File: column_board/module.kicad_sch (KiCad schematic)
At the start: 1 part, among them J2 J_MOD

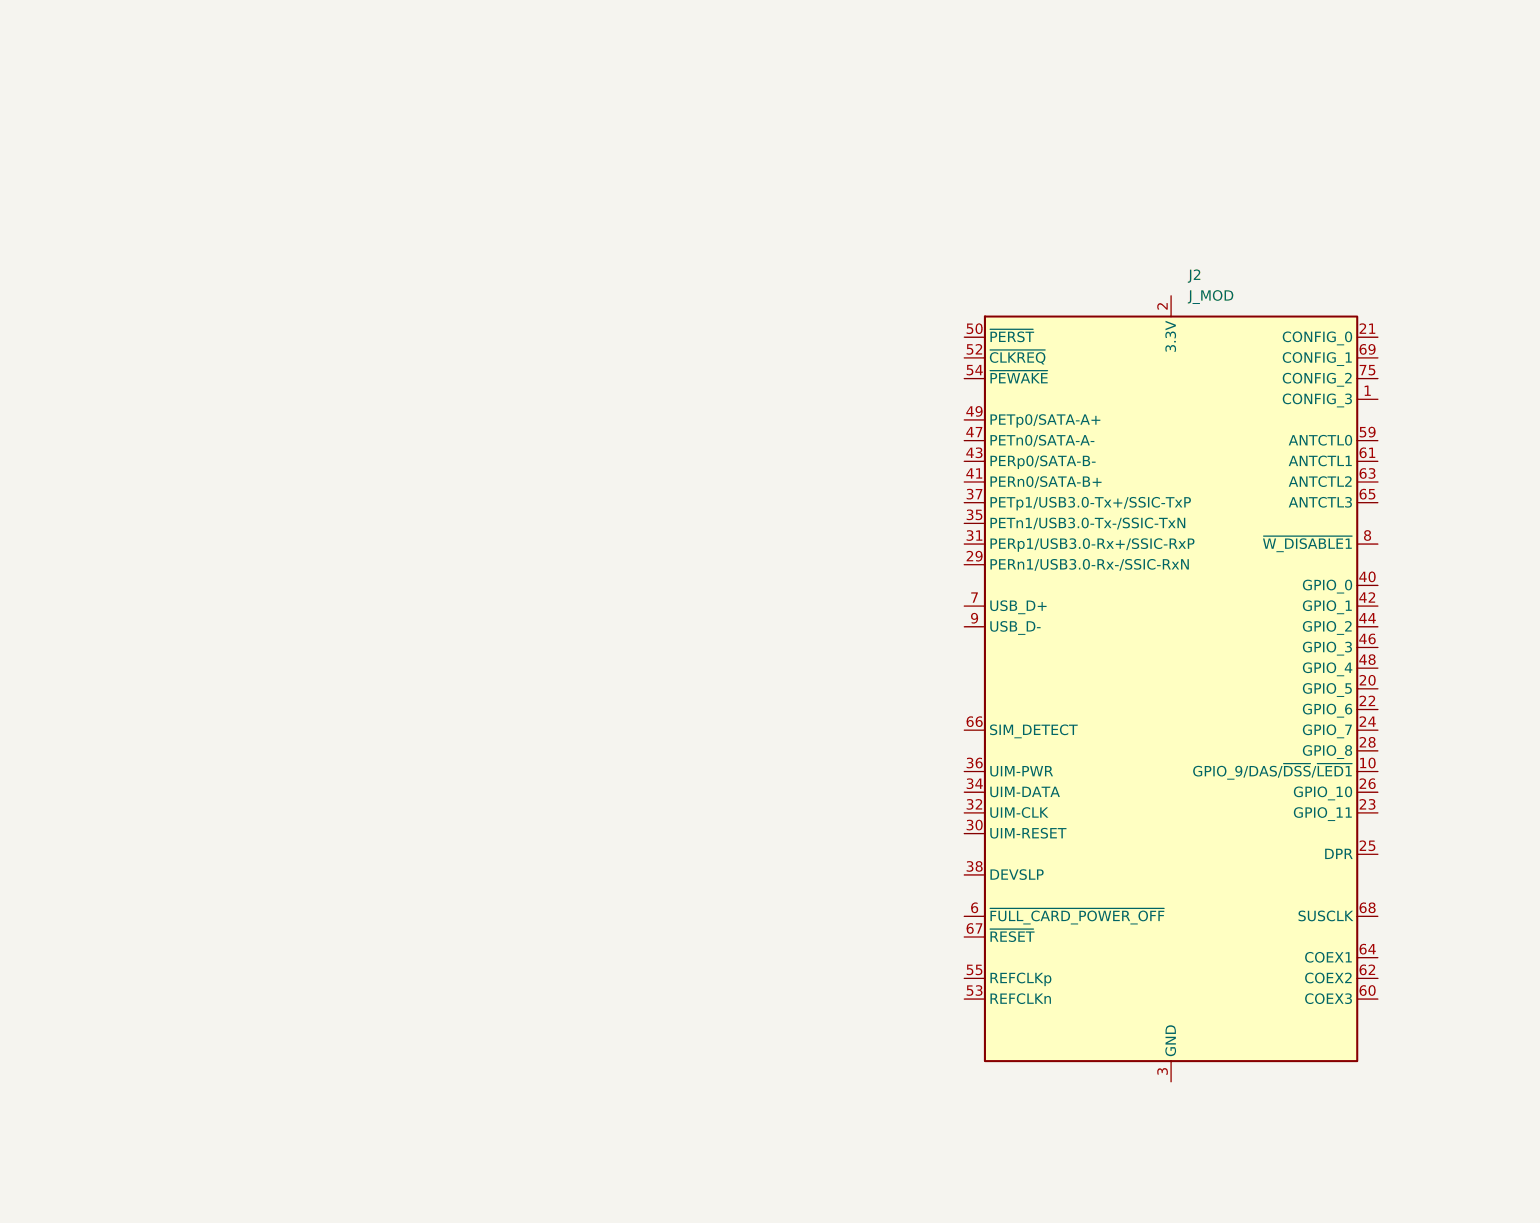
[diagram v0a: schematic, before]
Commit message: feat: create module connector system
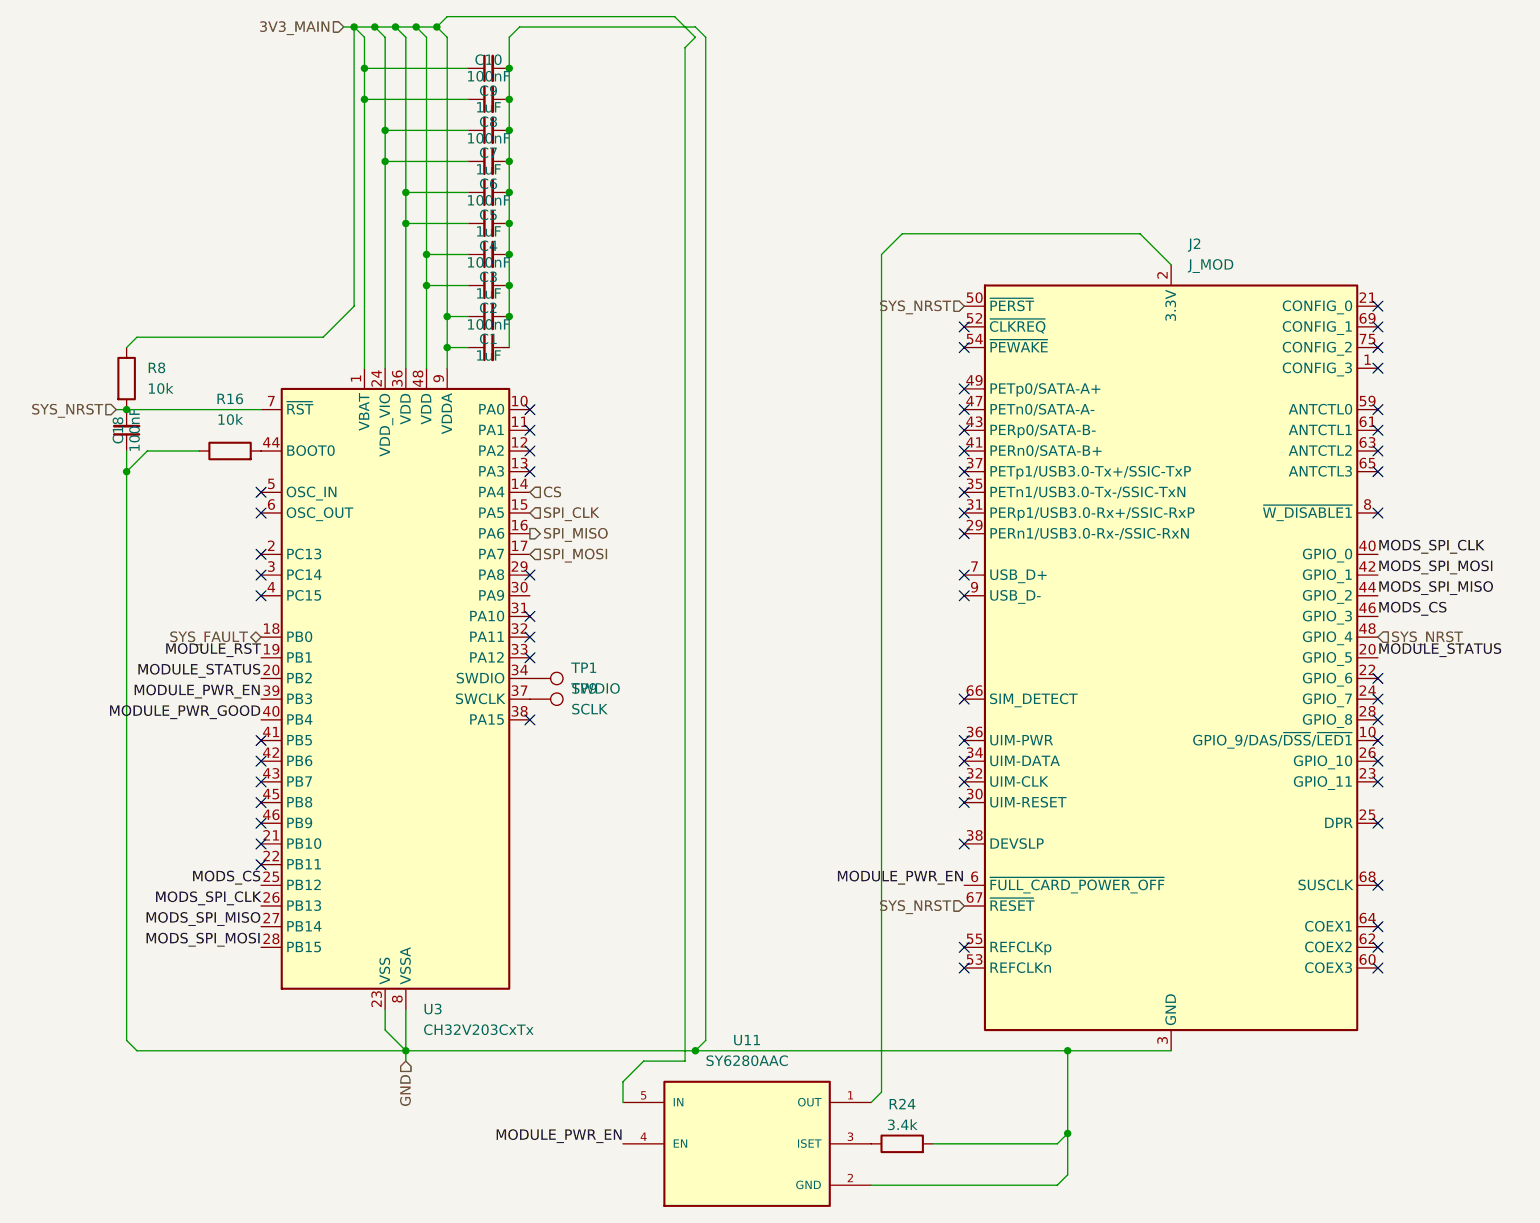
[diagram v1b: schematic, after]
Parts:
- added C1, C3, C5, C7, C9: 1uF, symbol Device:C_Small
- added C10, C18, C2, C4, C6, C8: 100nF, symbol Device:C_Small
- added R16, R8: 10k, symbol Device:R
- added R24: 3.4k, symbol Device:R
- added TP1: SWDIO, symbol Connector:TestPoint
- added TP9: SCLK, symbol Connector:TestPoint
- added U11: SY6280AAC, SY6280AAC:SOT95P285X130-5N, symbol SY6280AAC:SY6280AAC
- added U3: CH32V203CxTx, Package_QFP:LQFP-48_7x7mm_P0.5mm, symbol MCU_WCH_RiscV:CH32V203CxTx
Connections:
- net GND: now reaches J2.11 (GND), J2.27 (GND), J2.3 (GND), J2.33 (GND), J2.39 (GND), J2.45 (GND), J2.5 (GND), J2.51 (GND), J2.57 (GND), J2.71 (GND), J2.73 (GND)
- net GND: now also C1.2, C10.2, C18.1, C2.2, C3.2, C4.2, C5.2, C6.2, C7.2, C8.2, C9.2, R16.1, R24.2, U11.2 (GND), U3.23 (VSS), U3.35 (VSS), U3.47 (VSS), U3.8 (VSSA)
- net at J2.2 (3.3V), J2.4 (3.3V), J2.70 (3.3V)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: now also U11.1 (OUT)
- net MODULE_STATUS: now reaches J2.20 (GPIO_5)
- net MODULE_STATUS: now also U3.20 (PB2)
- net MODS_SPI_CLK: now reaches J2.40 (GPIO_0)
- net MODS_SPI_CLK: now also U3.26 (PB13)
- net MODS_SPI_MOSI: now reaches J2.42 (GPIO_1)
- net MODS_SPI_MOSI: now also U3.28 (PB15)
- net MODS_SPI_MISO: now reaches J2.44 (GPIO_2)
- net MODS_SPI_MISO: now also U3.27 (PB14)
- net MODS_CS: now reaches J2.46 (GPIO_3)
- net MODS_CS: now also U3.25 (PB12)
- net SYS_NRST: now reaches J2.48 (GPIO_4)
- net SYS_NRST: now also J2.50 (~{PERST}), J2.67 (~{RESET}), C18.2, R8.2, U3.7 (~{RST})
- net MODULE_PWR_EN: now reaches J2.6 (~{FULL_CARD_POWER_OFF})
- net MODULE_PWR_EN: now also U11.4 (EN), U3.39 (PB3)
- new net: R24.1, U11.3 (ISET)
- new net: TP1.1, U3.34 (SWDIO)
- new net: TP9.1, U3.37 (SWCLK)
- new net: R16.2, U3.44 (BOOT0)
- new net 3V3_MAIN: C1.1, C10.1, C2.1, C3.1, C4.1, C5.1, C6.1, C7.1, C8.1, C9.1, R8.1, U11.5 (IN), U3.1 (VBAT), U3.24 (VDD_VIO), U3.36 (VDD), U3.48 (VDD), U3.9 (VDDA)
- new net CS: U3.14 (PA4)
- new net MODULE_PWR_GOOD: U3.40 (PB4)
- new net MODULE_RST: U3.19 (PB1)
- new net SPI_CLK: U3.15 (PA5)
- new net SPI_MISO: U3.16 (PA6)
- new net SPI_MOSI: U3.17 (PA7)
- new net SYS_FAULT: U3.18 (PB0)
- no-connect marks 0 -> 61
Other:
- moved on the sheet: J2

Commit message: feat: start module board with daisy-chain SPI interface
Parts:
- removed C1, C3, C5, C7, C9: 1uF, symbol Device:C_Small
- removed C10, C2, C4, C6, C8: 100nF, symbol Device:C_Small
- added C19, C39, C57, C75, C91: 1uF, symbol Device:C_Small
- added C28, C38, C56, C74, C90: 100nF, symbol Device:C_Small
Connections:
- net 3V3_MAIN: now also C19.1, C28.1, C38.1, C39.1, C56.1, C57.1, C74.1, C75.1, C90.1, C91.1
- net GND: now also C19.2, C28.2, C38.2, C39.2, C56.2, C57.2, C74.2, C75.2, C90.2, C91.2
- net +3V3: now reaches J2.2 (3.3V), J2.4 (3.3V), J2.70 (3.3V), J2.72 (3.3V), J2.74 (3.3V), U11.1 (OUT)

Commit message: feat: finish all essential schematics (i think?)
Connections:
- net MODULE_PWR_EN: no longer J2.6 (~{FULL_CARD_POWER_OFF})
- no-connect marks 61 -> 62
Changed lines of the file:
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@@
+	)
+	(no_connect
+		(at 127 119.38)
 	)
 	(no_connect
@@
 		(effects
 			(font
-				(size 1.27 1.27)
-			)
-			(justify right bottom)
-		)
-	)
-	(label "MODULE_PWR_EN"
-		(at 127 119.38 180)
-		(effects
-			(font
